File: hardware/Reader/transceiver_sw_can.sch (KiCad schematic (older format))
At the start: 12 parts

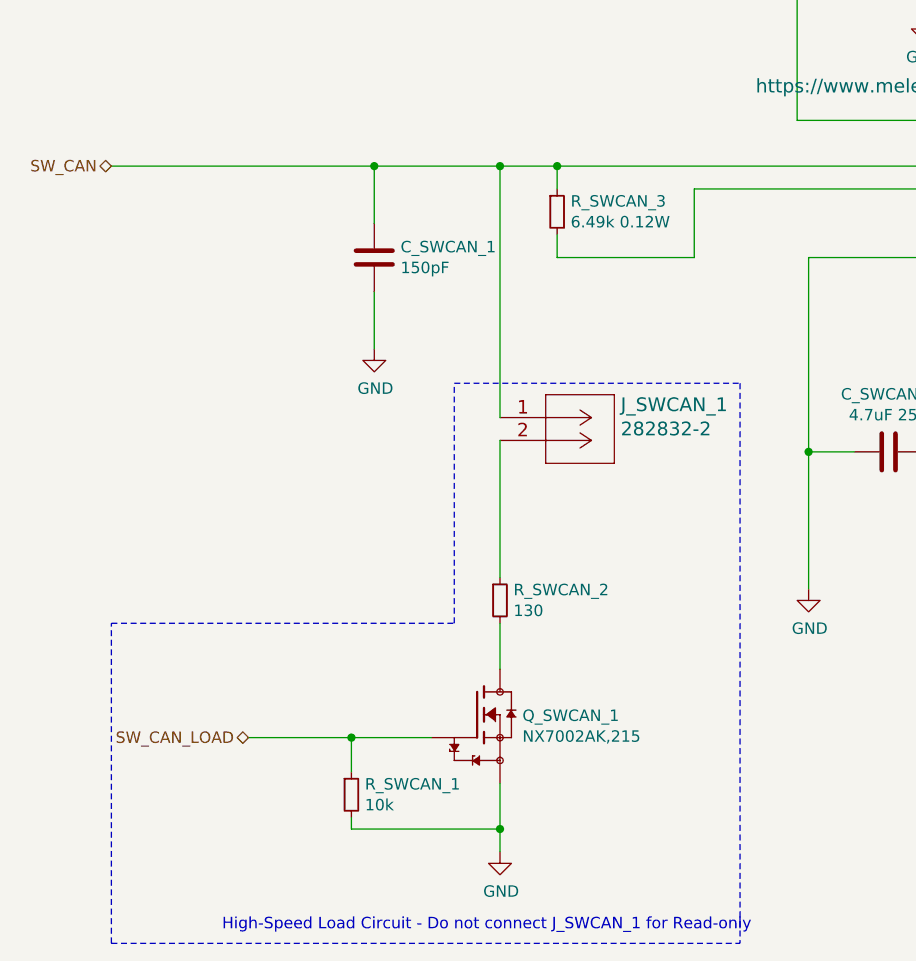
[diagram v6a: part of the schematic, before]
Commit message: Fixed bugs in schematic. Updated BOM list. Swapped to using ESP32 holder. Updated PCB layout to v0.0.2. Updated schematic to v0.0.4
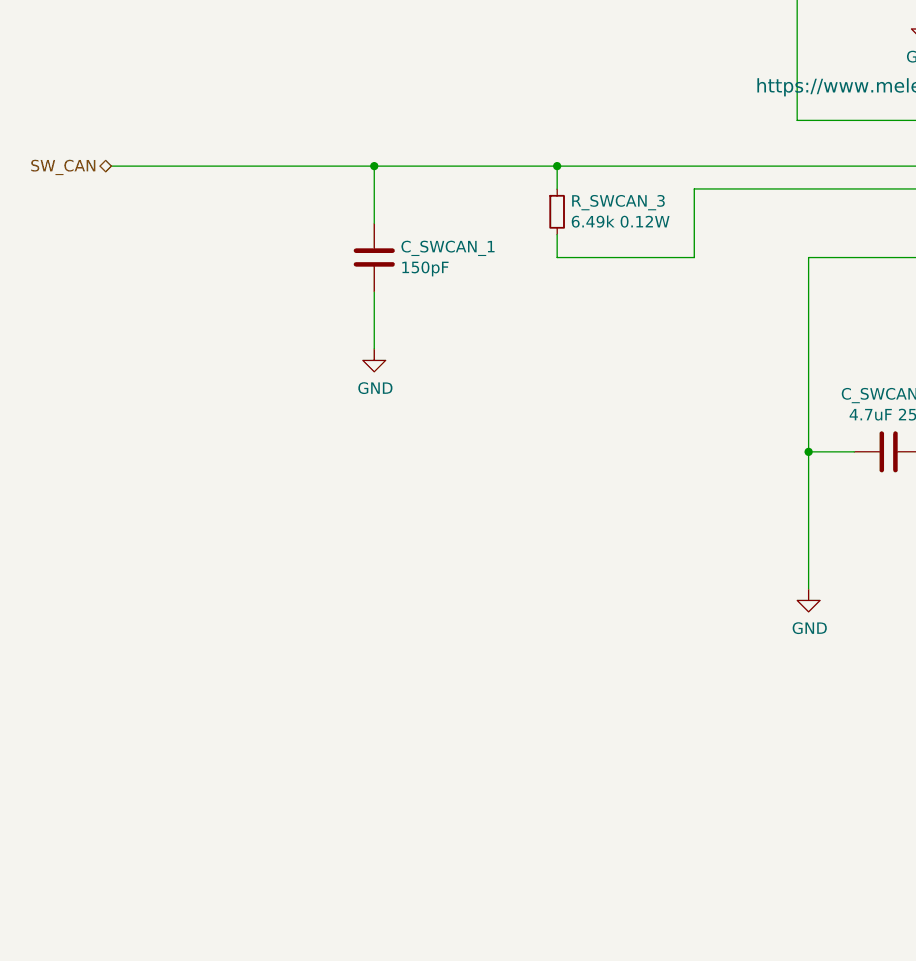
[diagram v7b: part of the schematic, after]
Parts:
- removed J_SWCAN_1: 282832-2, footprints:282832-2, symbol 2828322:282832-2
- removed Q_SWCAN_1: NX7002AK,215, footprints:SOT95P230X110-3N, symbol NX7002AK_215:NX7002AK,215
- removed R_SWCAN_1: 10k, footprints:RESC1608X55N, symbol Device:R_Small
- removed R_SWCAN_2: 130, footprints:RESC0603X26N, symbol Device:R_Small
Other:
- note removed: "High-Speed Load Circuit - Do not connect J_SWCAN_1 for Read-only"
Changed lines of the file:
@@
 Sheet 9 19
 Title "CANnect Reader | Single Wire CAN Transceiver"
-Date "2020-10-27"
-Rev "0.0.03"
+Date "2020-10-28"
+Rev "0.0.04"
 Comp "CANtech"
 Comment1 "Created by Choong Jin Ng | jin8383@gmail.com"
@@
 $EndComp
 $Comp
-L Device:R_Small R_SWCAN_2
-U 1 1 5FBCE6CE
-P 2600 4550
-F 0 "R_SWCAN_2" H 2659 4596 50  0000 L CNN
-F 1 "130" H 2659 4505 50  0000 L CNN
-F 2 "footprints:RESC0603X26N" H 2600 4550 50  0001 C CNN
-F 3 "https://www.yageo.com/upload/media/product/productsearch/datasheet/rchip/PYu-RC_Group_51_RoHS_L_11.pdf" H 2600 4550 50  0001 C CNN
-F 4 "RC0201FR-07130RL" H 2600 4550 50  0001 C CNN "Part Name"
-F 5 "Yageo" H 2600 4550 50  0001 C CNN "Manufacturer"
-F 6 "DigiKey Canada" H 2600 4550 50  0001 C CNN "Vendor"
-F 7 "YAG2394CT-ND" H 2600 4550 50  0001 C CNN "digikeypn"
-	1    2600 4550
-	1    0    0    -1
-$EndComp
-Text HLabel 1500 5150 0    50   BiDi ~ 0
-SW_CAN_LOAD
-$Comp
-L NX7002AK_215:NX7002AK,215 Q_SWCAN_1
-U 1 1 5FBCED49
-P 2500 5050
-F 0 "Q_SWCAN_1" H 2698 5046 50  0000 L CNN
-F 1 "NX7002AK,215" H 2698 4955 50  0000 L CNN
-F 2 "footprints:SOT95P230X110-3N" H 2500 5050 50  0001 L BNN
-F 3 "https://assets.nexperia.com/documents/data-sheet/NX7002AK.pdf" H 2500 5050 50  0001 L BNN
-F 4 "Nexperia" H 2500 5050 50  0001 L BNN "Field4"
-F 5 "7" H 2500 5050 50  0001 L BNN "Field5"
-F 6 "IPC-7351B" H 2500 5050 50  0001 L BNN "Field6"
-F 7 "NX7002AK,215" H 2500 5050 50  0001 C CNN "Part Name"
-F 8 "Nexperia USA Inc." H 2500 5050 50  0001 C CNN "Manufacturer"
-F 9 "DigiKey Canada" H 2500 5050 50  0001 C CNN "Vendor"
-F 10 "1727-1289-1-ND" H 2500 5050 50  0001 C CNN "digikeypn"
-	1    2500 5050
-	1    0    0    -1
-$EndComp
-$Comp
-L Device:R_Small R_SWCAN_1
-U 1 1 5FBCFFA6
-P 1950 5400
-F 0 "R_SWCAN_1" H 2009 5446 50  0000 L CNN
-F 1 "10k" H 2009 5355 50  0000 L CNN
-F 2 "footprints:RESC1608X55N" H 1950 5400 50  0001 C CNN
-F 3 "https://www.yageo.com/upload/media/product/productsearch/datasheet/rchip/PYu-RT_1-to-0.01_RoHS_L_12.pdf" H 1950 5400 50  0001 C CNN
-F 4 "RT0603FRE0710KL" H 1950 5400 50  0001 C CNN "Part Name"
-F 5 "Yageo" H 1950 5400 50  0001 C CNN "Manufacturer"
-F 6 "DigiKey Canada" H 1950 5400 50  0001 C CNN "Vendor"
-F 7 "YAG2321CT-ND" H 1950 5400 50  0001 C CNN "digikeypn"
-	1    1950 5400
-	1    0    0    -1
-$EndComp
-Wire Wire Line
-	1500 5150 1950 5150
-Wire Wire Line
-	1950 5300 1950 5150
-Connection ~ 1950 5150
-Wire Wire Line
-	1950 5150 2300 5150
-Wire Wire Line
-	2600 4850 2600 4650
-$Comp
-L power:GND #PWR047
-U 1 1 5FBD183F
-P 2600 5650
-F 0 "#PWR047" H 2600 5400 50  0001 C CNN
-F 1 "GND" H 2605 5477 50  0000 C CNN
-F 2 "" H 2600 5650 50  0001 C CNN
-F 3 "" H 2600 5650 50  0001 C CNN
-	1    2600 5650
-	1    0    0    -1
-$EndComp
-Wire Notes Line
-	900  6050 900  4650
-Wire Notes Line
-	900  4650 2400 4650
-Wire Notes Line
-	2400 4650 2400 3600
-Text Notes 3700 6000 2    50   ~ 0
-High-Speed Load Circuit - Do not connect J_SWCAN_1 for Read-only
-Wire Wire Line
-	2600 5350 2600 5550
-Wire Wire Line
-	1950 5500 1950 5550
-Wire Wire Line
-	1950 5550 2600 5550
-Connection ~ 2600 5550
-Wire Wire Line
-	2600 5550 2600 5650
-$Comp
 L Device:R_Small R_SWCAN_3
 U 1 1 5FBD3FD7
@@
 Wire Wire Line
 	8150 3600 8750 3600
-$Comp
-L 2828322:282832-2 J_SWCAN_1
-U 1 1 5F9F941C
-P 2600 3750
-F 0 "J_SWCAN_1" H 3128 3806 60  0000 L CNN
-F 1 "282832-2" H 3128 3700 60  0000 L CNN
-F 2 "footprints:282832-2" H 3000 3690 60  0001 C CNN
-F 3 "https://www.te.com/commerce/DocumentDelivery/DDEController?Action=srchrtrv&DocNm=282832&DocType=Customer+Drawing&DocLang=English" H 3128 3594 60  0001 L CNN
-F 4 "282832-2" H 2600 3750 50  0001 C CNN "Part Name"
-F 5 "DigiKey Canada" H 2600 3750 50  0001 C CNN "Vendor"
-F 6 "TE Connectivity AMP Connectors" H 2600 3750 50  0001 C CNN "Manufacturer"
-F 7 "A113314-ND" H 2600 3750 50  0001 C CNN "digikeypn"
-	1    2600 3750
-	1    0    0    -1
-$EndComp
-Wire Wire Line
-	2600 3750 2600 2650
-Connection ~ 2600 2650
-Wire Wire Line
-	2600 2650 2850 2650
-Wire Wire Line
-	2600 3850 2600 4450
 Wire Wire Line
 	3950 3050 4750 3050
 Wire Wire Line
 	4550 2850 4750 2850
-Wire Notes Line
-	2400 3600 3650 3600
-Wire Notes Line
-	3650 3600 3650 6050
-Wire Notes Line
-	900  6050 3650 6050
 Connection ~ 2050 2650
-Wire Wire Line
-	2050 2650 2600 2650
 Wire Wire Line
 	2050 3200 2050 3450
@@
 Wire Wire Line
 	900  2650 2050 2650
+Wire Wire Line
+	2050 2650 2850 2650
 $EndSCHEMATC

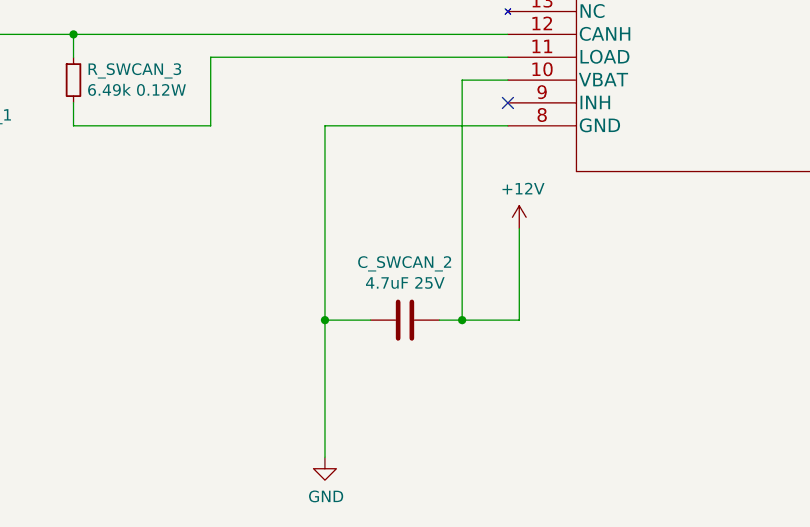
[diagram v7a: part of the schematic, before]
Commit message: Fixed a component name for header pin
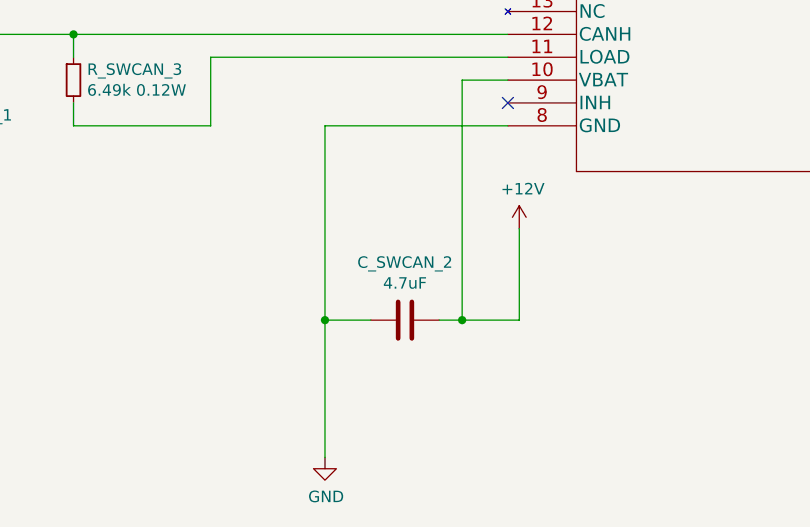
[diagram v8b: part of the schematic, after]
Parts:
- C_SWCAN_2: value 4.7uF 25V -> 4.7uF
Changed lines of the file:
@@
 P 4300 3900
 F 0 "C_SWCAN_2" V 4048 3900 50  0000 C CNN
-F 1 "4.7uF 25V" V 4139 3900 50  0000 C CNN
+F 1 "4.7uF" V 4139 3900 50  0000 C CNN
 F 2 "footprints:C1206C475K3RACAUTO" H 4338 3750 50  0001 C CNN
 F 3 "https://api.kemet.com/component-edge/download/specsheet/C1206C475K3RACAUTO.pdf" H 4300 3900 50  0001 C CNN
